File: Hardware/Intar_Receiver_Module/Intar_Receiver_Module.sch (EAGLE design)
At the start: 11 parts, among them J1 GROVE-4P-2.0-3470130P1, SW1 SWITCH_MOMENTARY

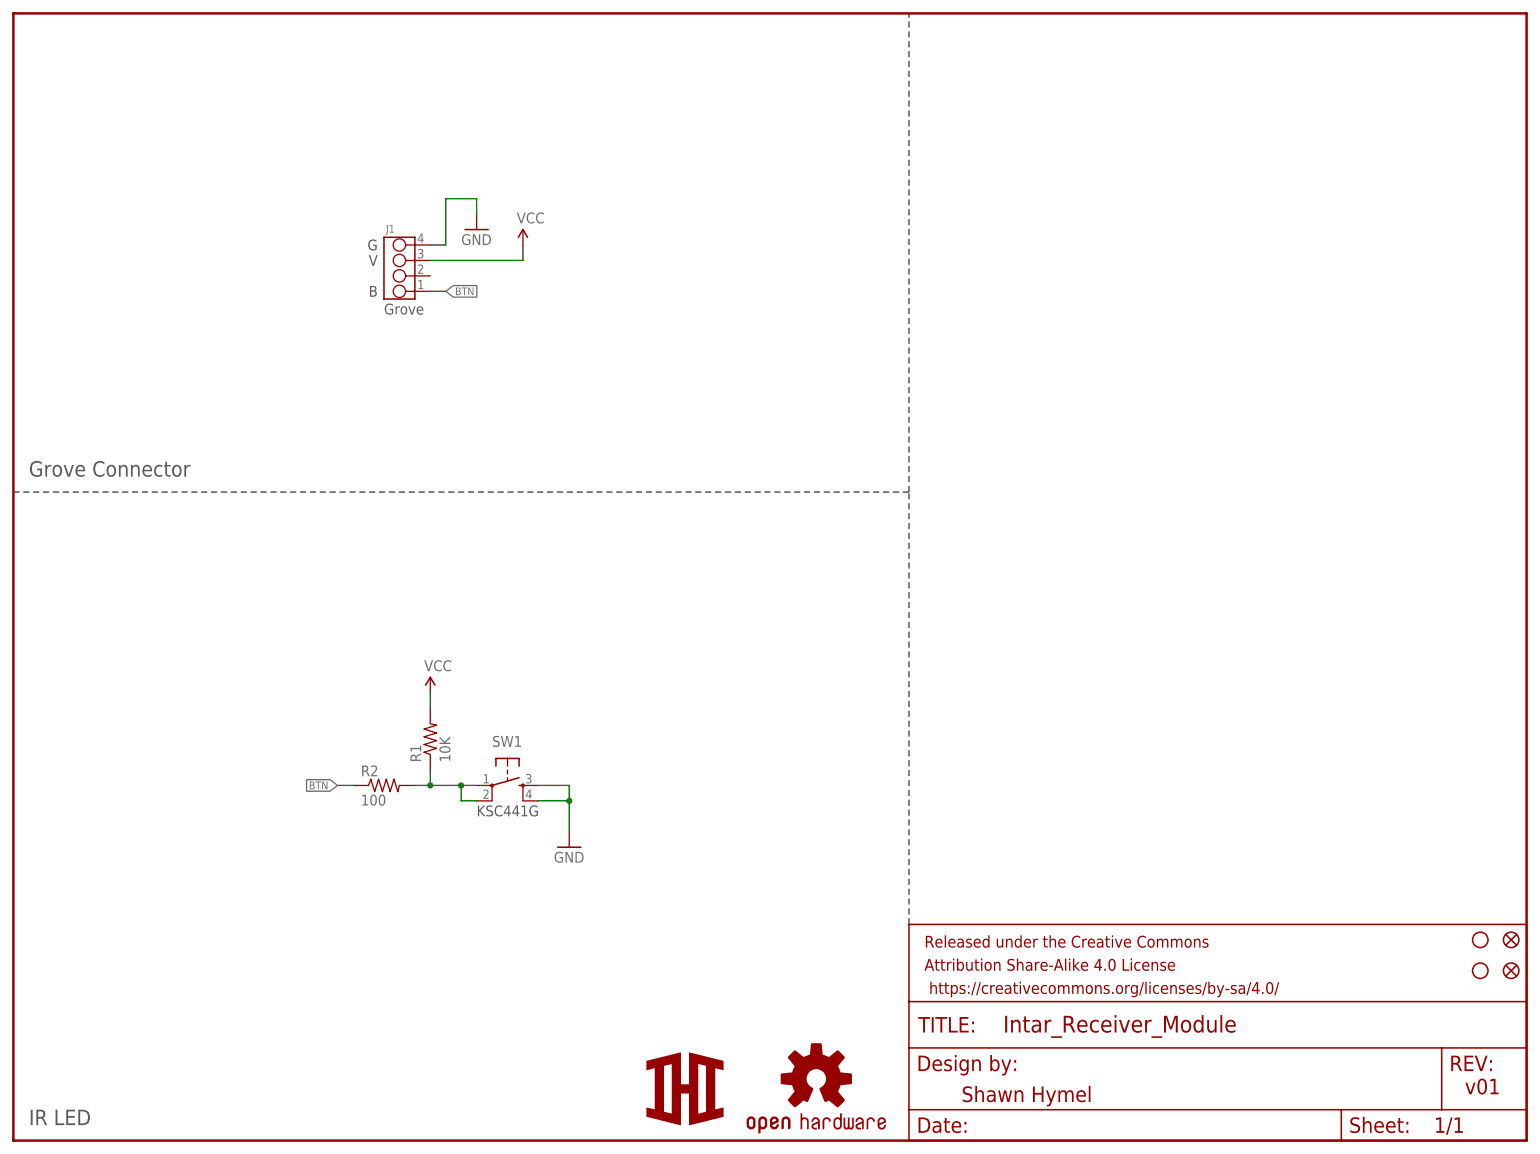
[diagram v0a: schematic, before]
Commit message: Created schematics for first round of modules.
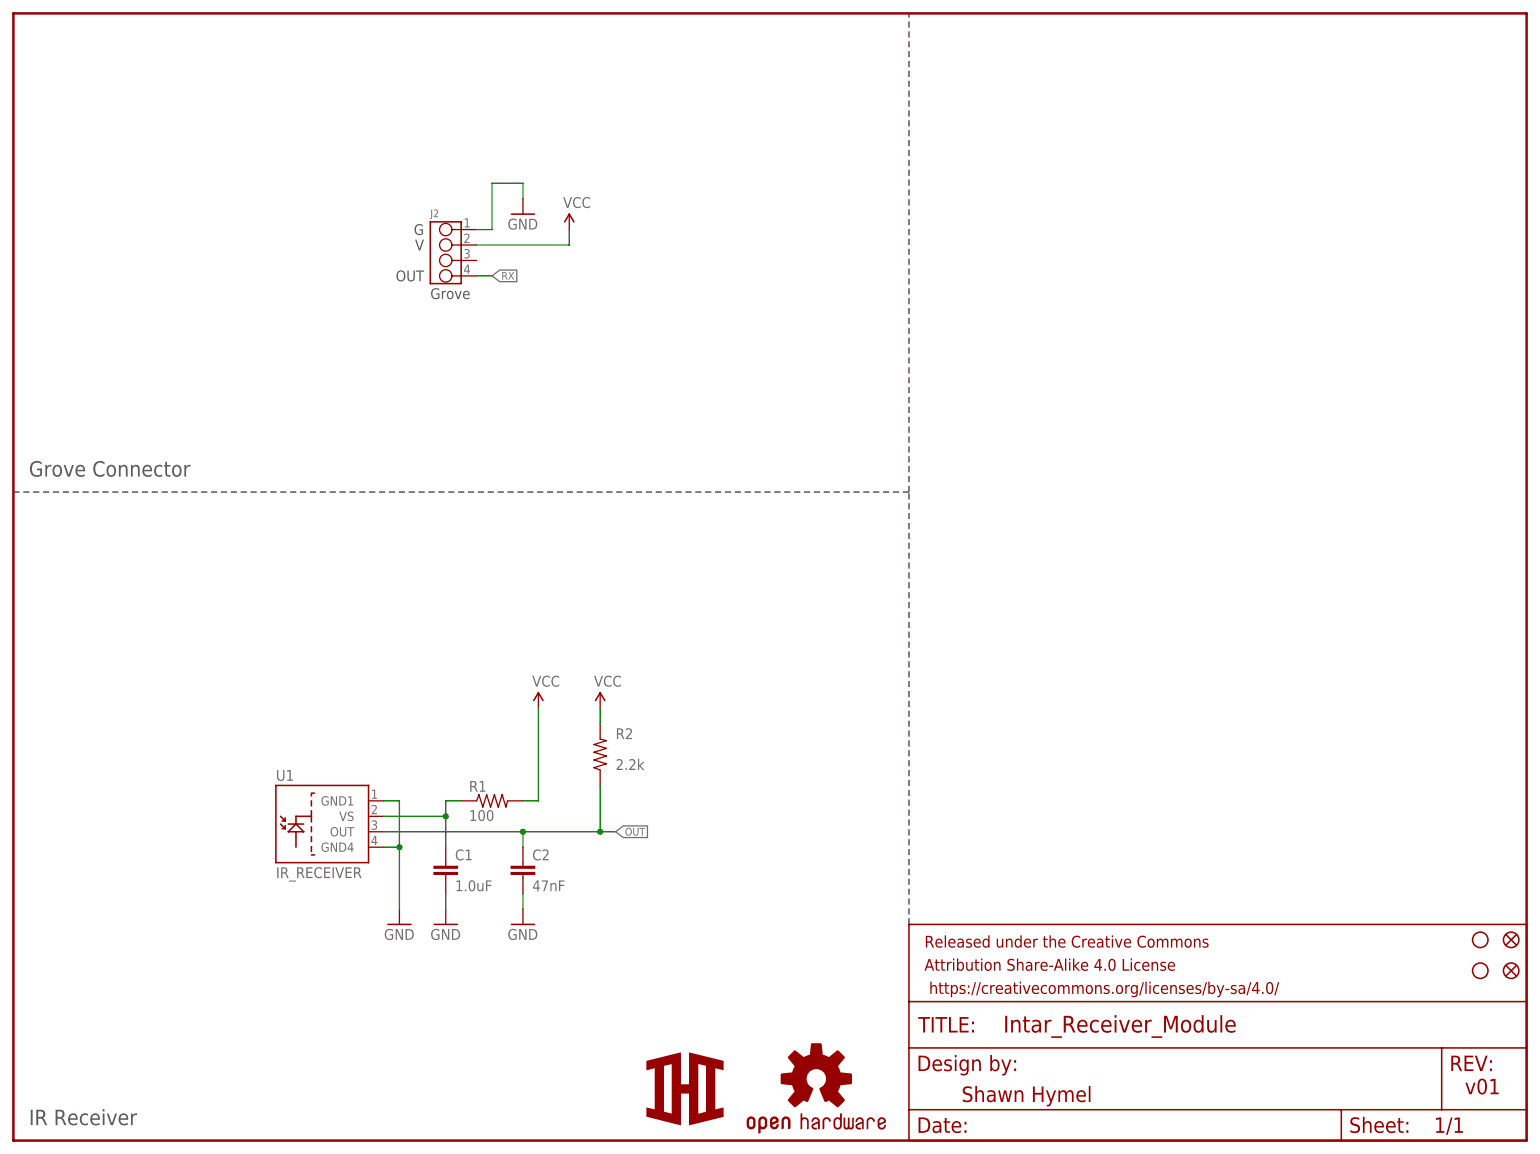
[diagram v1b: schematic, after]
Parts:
- removed J1: GROVE-4P-2.0-3470130P1, Connector:GROVE-4P-2.0-3470130P1
- removed SW1: SWITCH_MOMENTARY, Intar_Eagle_Library:SWITCH_MOMENTARY
- added C1: 1.0uF, SparkFun-Capacitors:1.0UF-16V-10%(0603)
- added C2: 47nF, SparkFun-Capacitors:47NF(0.047UF/47000PF)-25V-5%(0603)SMD
- added J2: GROVE-4P-2.0-3470130P1, Connector:GROVE-4P-2.0-3470130P1
- added U1: IR_RECEIVER, Intar_Eagle_Library:IR_RECEIVER
- R1: value 10K -> 100; device SparkFun-Resistors:10KOHM-1/10W-1%(0603)0603 -> SparkFun-Resistors:100OHM-1/10W-1%(0603)
- R2: value 100 -> 2.2k; device SparkFun-Resistors:100OHM-1/10W-1%(0603) -> SparkFun-Resistors:2.2KOHM-1/10W-1%(0603)
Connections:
- removed net BTN: J1.1, R2.1
- removed net N$1: R1.1, R2.2, SW1.1, SW1.2
- new net N$2: C1.1, R1.1, U1.VS
- new net OUT: C2.1, R2.1, U1.OUT
- new net RX: J2.4
- net GND: now also C1.2, C2.2, J2.1, U1.GND1, U1.GND4; no longer J1.4, SW1.3, SW1.4
- net VCC: now also J2.2, R2.2; no longer J1.3
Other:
- note added: "IR Receiver"
- note added: "OUT"
- note removed: "B"
- note removed: "IR LED"
- note removed: "KSC441G"
- moved on the sheet: R1, R2

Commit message: Arranged components on all modules
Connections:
- removed net RX: J2.4
- net OUT: now also J2.4
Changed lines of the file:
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@@
 <setting verticaltext="up"/>
 </settings>
-<grid distance="0.1" unitdist="inch" unit="inch" style="lines" multiple="1" display="yes" altdistance="0.01" altunitdist="inch" altunit="inch"/>
+<grid distance="0.1" unitdist="inch" unit="inch" style="lines" multiple="1" display="no" altdistance="0.01" altunitdist="inch" altunit="inch"/>
 <layers>
 <layer number="1" name="Top" color="4" fill="1" visible="no" active="no"/>
@@
 </segment>
 </net>
-<net name="RX" class="0">
-<segment>
-<pinref part="J2" gate="J" pin="4"/>
-<wire x1="76.2" y1="142.24" x2="78.74" y2="142.24" width="0.1524" layer="91"/>
-<label x="78.74" y="142.24" size="1.27" layer="95" xref="yes"/>
-</segment>
-</net>
 <net name="N$2" class="0">
 <segment>
@@
 <label x="99.06" y="50.8" size="1.27" layer="95" xref="yes"/>
 </segment>
+<segment>
+<pinref part="J2" gate="J" pin="4"/>
+<wire x1="76.2" y1="142.24" x2="78.74" y2="142.24" width="0.1524" layer="91"/>
+<label x="78.74" y="142.24" size="1.27" layer="95" xref="yes"/>
+</segment>
 </net>

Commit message: Fixed Grove connectors to be right way (pin 4 should be GND)
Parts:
- renumbered J2 to J1
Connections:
- net GND: now also J1.4; no longer J1.1
- net OUT: now also J1.1; no longer J1.4
- net VCC: now also J1.3; no longer J1.2
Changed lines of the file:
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@@
 <setting verticaltext="up"/>
 </settings>
-<grid distance="0.1" unitdist="inch" unit="inch" style="lines" multiple="1" display="no" altdistance="0.01" altunitdist="inch" altunit="inch"/>
+<grid distance="0.1" unitdist="inch" unit="inch" style="lines" multiple="1" display="yes" altdistance="0.01" altunitdist="inch" altunit="inch"/>
 <layers>
 <layer number="1" name="Top" color="4" fill="1" visible="no" active="no"/>
@@
 <part name="STANDOFF2" library="SparkFun-Electromechanical" deviceset="STAND-OFF" device=""/>
 <part name="LOGO1" library="SparkFun-Aesthetics" deviceset="OSHW-LOGO" device="S"/>
-<part name="J2" library="Connector" deviceset="GROVE-4P-2.0" device="-3470130P1"/>
 <part name="GND5" library="SparkFun-Aesthetics" deviceset="GND" device=""/>
 <part name="SUPPLY5" library="SparkFun-Aesthetics" deviceset="VCC" device=""/>
@@
 <part name="GND2" library="SparkFun-Aesthetics" deviceset="GND" device=""/>
 <part name="GND3" library="SparkFun-Aesthetics" deviceset="GND" device=""/>
+<part name="J1" library="Connector" deviceset="GROVE-4P-2.0" device="-3470130P1"/>
 </parts>
 <sheets>
@@
 <instance part="STANDOFF2" gate="G$1" x="241.3" y="27.94"/>
 <instance part="LOGO1" gate="G$1" x="132.08" y="10.16"/>
-<instance part="J2" gate="J" x="71.12" y="146.05" smashed="yes">
-<attribute name="NAME" x="68.58" y="151.892" size="1.27" layer="95" ratio="10"/>
-</instance>
 <instance part="GND5" gate="1" x="83.82" y="152.4"/>
 <instance part="SUPPLY5" gate="G$1" x="91.44" y="149.86"/>
@@
 <instance part="GND2" gate="1" x="71.12" y="35.56"/>
 <instance part="GND3" gate="1" x="83.82" y="35.56"/>
+<instance part="J1" gate="J" x="71.12" y="146.05" smashed="yes" rot="MR180">
+<attribute name="NAME" x="68.58" y="151.892" size="1.27" layer="95" ratio="10"/>
+</instance>
 </instances>
 <busses>
@@
 <net name="GND" class="0">
 <segment>
-<pinref part="J2" gate="J" pin="1"/>
 <wire x1="76.2" y1="149.86" x2="78.74" y2="149.86" width="0.1524" layer="91"/>
 <wire x1="78.74" y1="149.86" x2="78.74" y2="157.48" width="0.1524" layer="91"/>
@@
 <wire x1="83.82" y1="157.48" x2="83.82" y2="154.94" width="0.1524" layer="91"/>
 <pinref part="GND5" gate="1" pin="GND"/>
+<pinref part="J1" gate="J" pin="4"/>
 </segment>
 <segment>
@@
 <net name="VCC" class="0">
 <segment>
-<pinref part="J2" gate="J" pin="2"/>
 <wire x1="76.2" y1="147.32" x2="91.44" y2="147.32" width="0.1524" layer="91"/>
 <wire x1="91.44" y1="147.32" x2="91.44" y2="149.86" width="0.1524" layer="91"/>
 <pinref part="SUPPLY5" gate="G$1" pin="VCC"/>
+<pinref part="J1" gate="J" pin="3"/>
 </segment>
 <segment>
@@
 </segment>
 <segment>
-<pinref part="J2" gate="J" pin="4"/>
 <wire x1="76.2" y1="142.24" x2="78.74" y2="142.24" width="0.1524" layer="91"/>
 <label x="78.74" y="142.24" size="1.27" layer="95" xref="yes"/>
+<pinref part="J1" gate="J" pin="1"/>
 </segment>
 </net>
